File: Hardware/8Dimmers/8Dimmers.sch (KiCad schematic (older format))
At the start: 73 parts, among them J1 ISP, P10 CONN_01X02, P11 5VIN, P2 CONN_01X02, P3 CONN_01X02, P4 CONN_01X02, P5 CONN_01X02, P6 CONN_01X02, P7 CONN_01X02, P8 CONN_01X02, P9 CONN_01X02, SW1 RST, SW2 FLASH, U1 LTV-814, U10 MOC3023M, U11 MOC3023M, U12 MOC3023M, U13 MOC3023M, U14 TRIAC_small, U15 TRIAC_small, U16 TRIAC_small, U17 TRIAC_small, U18 TRIAC_small, U19 TRIAC_small, U2 AP1117D33, U20 TRIAC_small, U21 TRIAC_small, U3 ESP-12F, U4 74HC595, U5 ULN2803A, U6 MOC3023M, U7 MOC3023M, U8 MOC3023M, U9 MOC3023M

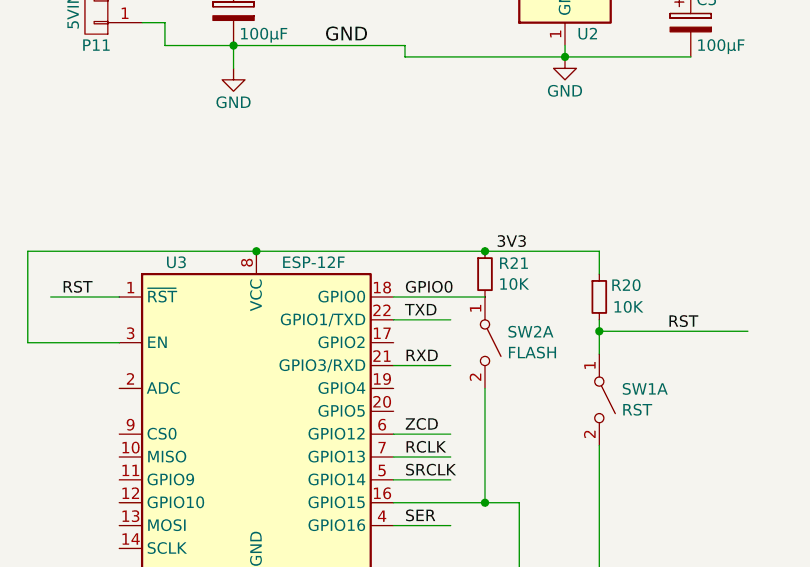
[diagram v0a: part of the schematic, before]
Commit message: - Modified almost all hardware boards : They were missing a pull-up resistor on GPIO2, which made impossible to flash. - Updated baseBoard.* files
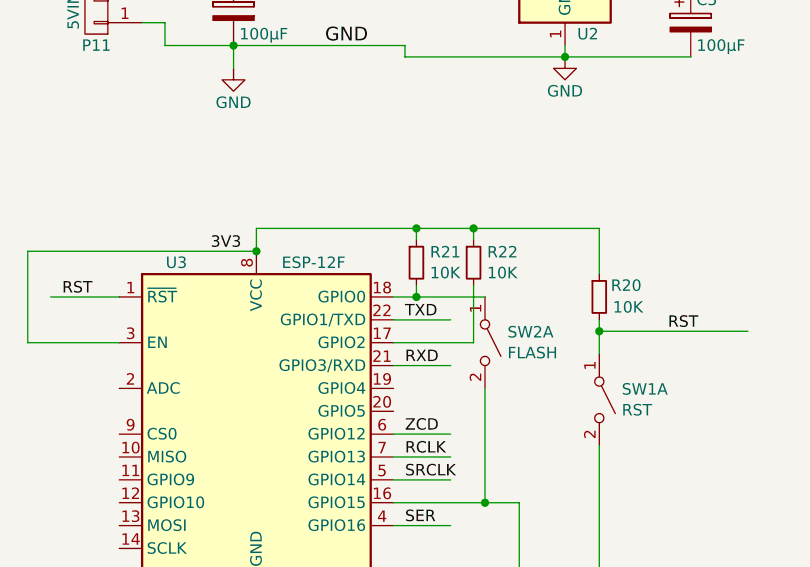
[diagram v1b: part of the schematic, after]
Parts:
- added R22: 10K, Resistor_SMD:R_0805_2012Metric_Pad1.15x1.40mm_HandSolder, symbol 8Dimmers-rescue:R_Small
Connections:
- net labels removed: GPIO0
- wire segments 189 -> 197
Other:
- moved on the sheet: R21
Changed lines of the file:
@@
 Wire Wire Line
 	700  2450 1100 2450
-Connection ~ 1700 2050
 Wire Wire Line
 	800  2250 1100 2250
@@
 Wire Wire Line
 	3200 2400 3200 2500
-Wire Wire Line
-	3200 2150 3200 2050
-Wire Wire Line
-	3200 2050 2700 2050
 Wire Wire Line
 	3200 2900 3200 3550
@@
 Text Label 2350 2950 0    50   ~ 0
 RCLK
-Text Label 2750 2050 0    50   ~ 0
+Text Label 1500 2050 0    50   ~ 0
 3V3
 $Comp
 L 8Dimmers-rescue:R_Small R21
 U 1 1 5BAEE165
-P 2700 2150
-F 0 "R21" H 2759 2196 50  0000 L CNN
-F 1 "10K" H 2759 2105 50  0000 L CNN
-F 2 "Resistor_SMD:R_0805_2012Metric_Pad1.15x1.40mm_HandSolder" H 2700 2150 50  0001 C CNN
-F 3 "" H 2700 2150 50  0000 C CNN
-	1    2700 2150
+P 2400 2100
+F 0 "R21" H 2459 2146 50  0000 L CNN
+F 1 "10K" H 2459 2055 50  0000 L CNN
+F 2 "Resistor_SMD:R_0805_2012Metric_Pad1.15x1.40mm_HandSolder" H 2400 2100 50  0001 C CNN
+F 3 "" H 2400 2100 50  0000 C CNN
+	1    2400 2100
 	1    0    0    -1
 $EndComp
-Connection ~ 2700 2050
 Wire Wire Line
-	1700 2050 2700 2050
-Wire Wire Line
-	2300 2250 2700 2250
+	2300 2250 2400 2250
 $Comp
 L Connector:Conn_01x04_Male J1
@@
 Text Label 2350 2550 0    50   ~ 0
 RXD
-Text Label 2350 2250 0    50   ~ 0
-GPIO0
 $Comp
 L Switch:SW_DPST_x2 SW2
@@
 Wire Wire Line
 	2700 3150 2850 3150
+$Comp
+L 8Dimmers-rescue:R_Small R22
+U 1 1 5C86ECA3
+P 2650 2100
+F 0 "R22" H 2709 2146 50  0000 L CNN
+F 1 "10K" H 2709 2055 50  0000 L CNN
+F 2 "Resistor_SMD:R_0805_2012Metric_Pad1.15x1.40mm_HandSolder" H 2650 2100 50  0001 C CNN
+F 3 "" H 2650 2100 50  0000 C CNN
+	1    2650 2100
+	1    0    0    -1
+$EndComp
+Wire Wire Line
+	2400 2250 2400 2200
+Connection ~ 2400 2250
+Wire Wire Line
+	2400 2250 2700 2250
+Wire Wire Line
+	2650 2200 2650 2450
+Wire Wire Line
+	2650 2450 2300 2450
+Wire Wire Line
+	3200 1950 2650 1950
+Wire Wire Line
+	1700 1950 1700 2050
+Wire Wire Line
+	3200 1950 3200 2150
+Connection ~ 1700 2050
+Wire Wire Line
+	2400 2000 2400 1950
+Connection ~ 2400 1950
+Wire Wire Line
+	2400 1950 1700 1950
+Wire Wire Line
+	2650 2000 2650 1950
+Connection ~ 2650 1950
+Wire Wire Line
+	2650 1950 2400 1950
 $EndSCHEMATC
